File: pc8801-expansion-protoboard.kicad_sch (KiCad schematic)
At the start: 48 parts, among them J1 Solder Side, J10 CPOL select (to Fuji), J11 CPOL (Latch), J2 Parts Side, J3 5V, J4 12V, J5 -12V, J6 GND_1, J7 GND_2, J8 CPOL select (ESP)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

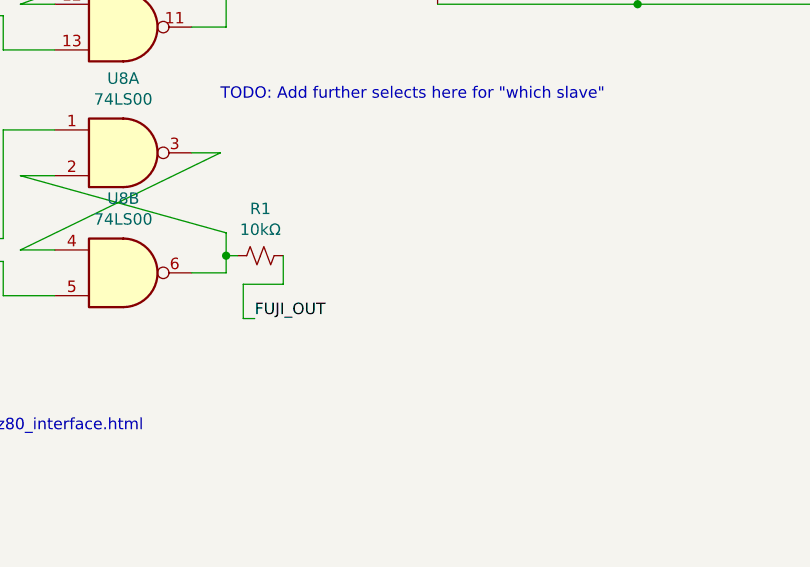
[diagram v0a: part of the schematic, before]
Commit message: Jumper to disable PU/PD
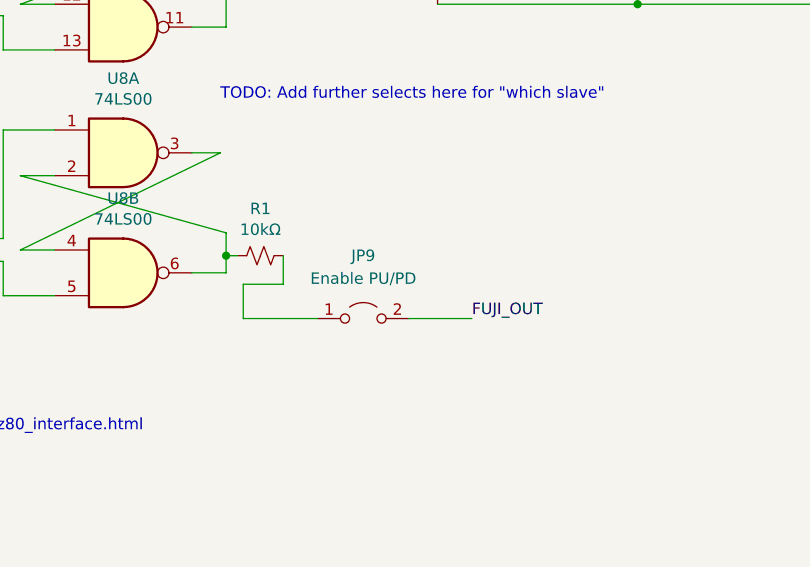
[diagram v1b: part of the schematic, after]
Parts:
- added JP9: Enable PU/PD, Connector_PinHeader_2.54mm:PinHeader_1x02_P2.54mm_Vertical, symbol Jumper:Jumper_2_Open
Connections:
- net FUJI_OUT: now also JP9.2 (B); no longer R1.2
- new net: JP9.1 (A), R1.2
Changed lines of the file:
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@@
+    (stroke (width 0) (type default) (color 0 0 0 0))
+  )
+  (wire (pts (xy 184.15 193.675) (xy 191.135 193.675))
     (stroke (width 0) (type default) (color 0 0 0 0))
   )
@@
     (stroke (width 0) (type default) (color 0 0 0 0))
   )
-  (wire (pts (xy 167.005 193.675) (xy 165.735 193.675))
+  (wire (pts (xy 165.735 193.675) (xy 173.99 193.675))
     (stroke (width 0) (type default) (color 0 0 0 0))
   )
@@
     (effects (font (size 1.27 1.27)) (justify left bottom))
   )
+  (label "FUJI_OUT" (at 191.135 193.675 0)
+    (effects (font (size 1.27 1.27)) (justify left bottom))
+  )
   (label "D1" (at 238.125 82.55 180)
     (effects (font (size 1.27 1.27)) (justify right bottom))
@@
   )
   (label "GND" (at 187.325 158.75 0)
-    (effects (font (size 1.27 1.27)) (justify left bottom))
-  )
-  (label "FUJI_OUT" (at 167.005 193.675 0)
     (effects (font (size 1.27 1.27)) (justify left bottom))
   )
@@
     (pin "3")
   )
+  (symbol (lib_id "Jumper:Jumper_2_Open") (at 179.07 193.675 0) (unit 1)
+    (in_bom yes) (on_board yes) (fields_autoplaced)
+    (property "Reference" "JP9" (id 0) (at 179.07 186.69 0))
+    (property "Value" "Enable PU/PD" (id 1) (at 179.07 189.23 0))
+    (property "Footprint" "Connector_PinHeader_2.54mm:PinHeader_1x02_P2.54mm_Vertical" (id 2) (at 179.07 193.675 0)
+      (effects (font (size 1.27 1.27)) hide)
+    )
+    (property "Datasheet" "~" (id 3) (at 179.07 193.675 0)
+      (effects (font (size 1.27 1.27)) hide)
+    )
+    (pin "1")
+    (pin "2")
+  )
   (symbol (lib_id "Device:D") (at 78.105 227.33 0) (unit 1)
     (in_bom yes) (on_board yes) (fields_autoplaced)
@@
       (reference "JP8") (unit 1) (value "Jumper_NC_Small") (footprint "Jumper:SolderJumper-2_P1.3mm_Bridged_RoundedPad1.0x1.5mm")
     )
+    (path "/a6a5797b-18fe-4a42-aa73-fdaee054c816"
+      (reference "JP9") (unit 1) (value "Enable PU/PD") (footprint "Connector_PinHeader_2.54mm:PinHeader_1x02_P2.54mm_Vertical")
+    )
     (path "/00000000-0000-0000-0000-000062ccaf1b"

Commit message: Test hooks for SPI clock
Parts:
- added TP3: SPI Clock, TestPoint:TestPoint_Loop_D2.60mm_Drill1.4mm_Beaded, symbol Connector:TestPoint
- added TP4: ~{SPI Clock}, TestPoint:TestPoint_Loop_D2.60mm_Drill1.4mm_Beaded, symbol Connector:TestPoint
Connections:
- net SPI_CLK: now also TP3.1
- net ~{SPI_CLK}: now also TP4.1
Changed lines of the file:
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@@
+    (stroke (width 0) (type default) (color 0 0 0 0))
+  )
+  (wire (pts (xy 271.78 30.48) (xy 271.78 36.195))
     (stroke (width 0) (type default) (color 0 0 0 0))
   )
@@
   )
   (wire (pts (xy 231.14 56.515) (xy 231.14 90.805))
+    (stroke (width 0) (type default) (color 0 0 0 0))
+  )
+  (wire (pts (xy 288.29 30.48) (xy 288.29 36.195))
     (stroke (width 0) (type default) (color 0 0 0 0))
   )
@@
     (effects (font (size 1.27 1.27)) (justify left bottom))
   )
+  (label "SPI_CLK" (at 271.78 36.195 270)
+    (effects (font (size 1.27 1.27)) (justify right bottom))
+  )
   (label "~{RESET}" (at 59.69 215.9 180)
     (effects (font (size 1.27 1.27)) (justify right bottom))
@@
   (label "GND" (at 254 120.65 0)
     (effects (font (size 1.27 1.27)) (justify left bottom))
+  )
+  (label "~{SPI_CLK}" (at 288.29 36.195 270)
+    (effects (font (size 1.27 1.27)) (justify right bottom))
   )
   (label "A0" (at 104.14 157.48 180)
@@
     (pin "1")
   )
+  (symbol (lib_id "Connector:TestPoint") (at 288.29 30.48 0) (unit 1)
+    (in_bom yes) (on_board yes) (fields_autoplaced)
+    (property "Reference" "TP4" (id 0) (at 290.83 25.9079 0)
+      (effects (font (size 1.27 1.27)) (justify left))
+    )
+    (property "Value" "~{SPI Clock}" (id 1) (at 290.83 29.0829 0)
+      (effects (font (size 1.27 1.27)) (justify left))
+    )
+    (property "Footprint" "TestPoint:TestPoint_Loop_D2.60mm_Drill1.4mm_Beaded" (id 2) (at 293.37 30.48 0)
+      (effects (font (size 1.27 1.27)) hide)
+    )
+    (property "Datasheet" "~" (id 3) (at 293.37 30.48 0)
+      (effects (font (size 1.27 1.27)) hide)
+    )
+    (pin "1")
+  )
   (symbol (lib_id "Connector:TestPoint") (at 63.5 27.305 0) (unit 1)
     (in_bom yes) (on_board yes) (fields_autoplaced)
@@
     (pin "2")
   )
+  (symbol (lib_id "Connector:TestPoint") (at 271.78 30.48 0) (unit 1)
+    (in_bom yes) (on_board yes) (fields_autoplaced)
+    (property "Reference" "TP3" (id 0) (at 274.32 25.9079 0)
+      (effects (font (size 1.27 1.27)) (justify left))
+    )
+    (property "Value" "SPI Clock" (id 1) (at 274.32 28.4479 0)
+      (effects (font (size 1.27 1.27)) (justify left))
+    )
+    (property "Footprint" "TestPoint:TestPoint_Loop_D2.60mm_Drill1.4mm_Beaded" (id 2) (at 276.86 30.48 0)
+      (effects (font (size 1.27 1.27)) hide)
+    )
+    (property "Datasheet" "~" (id 3) (at 276.86 30.48 0)
+      (effects (font (size 1.27 1.27)) hide)
+    )
+    (pin "1")
+  )
   (symbol (lib_id "Device:D") (at 78.105 227.33 0) (unit 1)
     (in_bom yes) (on_board yes) (fields_autoplaced)
@@
       (reference "TP2") (unit 1) (value "TestPoint") (footprint "TestPoint:TestPoint_Loop_D2.60mm_Drill1.4mm_Beaded")
     )
+    (path "/ce9231c3-ef0f-4298-8666-3e023bba7902"
+      (reference "TP3") (unit 1) (value "SPI Clock") (footprint "TestPoint:TestPoint_Loop_D2.60mm_Drill1.4mm_Beaded")
+    )
+    (path "/01b34e41-af93-4e1d-928b-489fa2be9377"
+      (reference "TP4") (unit 1) (value "~{SPI Clock}") (footprint "TestPoint:TestPoint_Loop_D2.60mm_Drill1.4mm_Beaded")
+    )
     (path "/00000000-0000-0000-0000-000061c04125"

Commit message: Series 220uF on 5V
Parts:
- added C?: 220µF, Capacitor_THT:CP_Radial_D5.0mm_P2.00mm, symbol Device:C_Polarized_Small_US
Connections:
- net +5V: now also C?.1; no longer J1.3 (Pin_3), J1.4 (Pin_4), J2.3 (Pin_3), J2.4 (Pin_4), U1.3A (+5V), U1.3B (+5V), U1.4A (+5V), U1.4B (+5V)
- new net 5V_RAW: C?.2, J1.3 (Pin_3), J1.4 (Pin_4), J2.3 (Pin_3), J2.4 (Pin_4), U1.3A (+5V), U1.3B (+5V), U1.4A (+5V), U1.4B (+5V)
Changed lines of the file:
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@@
   (junction (at 187.325 234.315) (diameter 0) (color 0 0 0 0)
   )
-  (junction (at 178.435 53.34) (diameter 0) (color 0 0 0 0)
-  )
   (junction (at 135.89 70.485) (diameter 0) (color 0 0 0 0)
   )
   (junction (at 51.435 140.97) (diameter 0) (color 0 0 0 0)
   )
+  (junction (at 122.555 52.705) (diameter 0) (color 0 0 0 0)
+  )
   (junction (at 158.75 47.625) (diameter 0) (color 0 0 0 0)
   )
@@
   (junction (at 282.575 74.295) (diameter 0) (color 0 0 0 0)
   )
-  (junction (at 122.555 52.705) (diameter 0) (color 0 0 0 0)
-  )
   (junction (at 158.75 106.045) (diameter 0) (color 0 0 0 0)
   )
@@
   (junction (at 250.825 120.65) (diameter 0) (color 0 0 0 0)
   )
+  (junction (at 97.155 36.195) (diameter 0) (color 0 0 0 0)
+  )
   (junction (at 135.89 65.405) (diameter 0) (color 0 0 0 0)
-  )
-  (junction (at 122.555 53.975) (diameter 0) (color 0 0 0 0)
   )
   (junction (at 82.55 257.81) (diameter 0) (color 0 0 0 0)
@@
     (stroke (width 0) (type default) (color 0 0 0 0))
   )
-  (wire (pts (xy 180.975 53.34) (xy 178.435 53.34))
-    (stroke (width 0) (type default) (color 0 0 0 0))
-  )
   (wire (pts (xy 129.54 160.02) (xy 139.065 160.02))
     (stroke (width 0) (type default) (color 0 0 0 0))
@@
     (stroke (width 0) (type default) (color 0 0 0 0))
   )
+  (wire (pts (xy 97.155 36.195) (xy 102.235 36.195))
+    (stroke (width 0) (type default) (color 0 0 0 0))
+  )
   (wire (pts (xy 167.005 124.46) (xy 167.005 128.905))
     (stroke (width 0) (type default) (color 0 0 0 0))
   )
+  (wire (pts (xy 93.345 36.195) (xy 97.155 36.195))
+    (stroke (width 0) (type default) (color 0 0 0 0))
+  )
   (wire (pts (xy 192.405 250.825) (xy 192.405 245.11))
     (stroke (width 0) (type default) (color 0 0 0 0))
@@
     (stroke (width 0) (type default) (color 0 0 0 0))
   )
-  (wire (pts (xy 122.555 55.245) (xy 122.555 53.975))
-    (stroke (width 0) (type default) (color 0 0 0 0))
-  )
   (wire (pts (xy 139.065 160.02) (xy 139.065 163.83))
     (stroke (width 0) (type default) (color 0 0 0 0))
@@
     (stroke (width 0) (type default) (color 0 0 0 0))
   )
-  (wire (pts (xy 120.015 53.975) (xy 122.555 53.975))
-    (stroke (width 0) (type default) (color 0 0 0 0))
-  )
   (wire (pts (xy 129.54 162.56) (xy 138.43 162.56))
     (stroke (width 0) (type default) (color 0 0 0 0))
@@
     (stroke (width 0) (type default) (color 0 0 0 0))
   )
-  (wire (pts (xy 178.435 55.245) (xy 178.435 53.34))
-    (stroke (width 0) (type default) (color 0 0 0 0))
-  )
   (wire (pts (xy 213.36 65.405) (xy 213.36 83.185))
     (stroke (width 0) (type default) (color 0 0 0 0))
@@
     (stroke (width 0) (type default) (color 0 0 0 0))
   )
+  (wire (pts (xy 122.555 36.195) (xy 122.555 52.705))
+    (stroke (width 0) (type default) (color 0 0 0 0))
+  )
   (wire (pts (xy 178.435 131.445) (xy 178.435 133.35))
     (stroke (width 0) (type default) (color 0 0 0 0))
@@
     (stroke (width 0) (type default) (color 0 0 0 0))
   )
+  (wire (pts (xy 107.315 36.195) (xy 122.555 36.195))
+    (stroke (width 0) (type default) (color 0 0 0 0))
+  )
   (wire (pts (xy 122.555 65.405) (xy 135.89 65.405))
     (stroke (width 0) (type default) (color 0 0 0 0))
@@
     (stroke (width 0) (type default) (color 0 0 0 0))
   )
-  (wire (pts (xy 178.435 53.34) (xy 178.435 52.705))
-    (stroke (width 0) (type default) (color 0 0 0 0))
-  )
-  (wire (pts (xy 122.555 53.975) (xy 122.555 52.705))
+  (wire (pts (xy 178.435 52.705) (xy 178.435 55.245))
+    (stroke (width 0) (type default) (color 0 0 0 0))
+  )
+  (wire (pts (xy 122.555 52.705) (xy 122.555 55.245))
     (stroke (width 0) (type default) (color 0 0 0 0))
   )
@@
     (effects (font (size 1.27 1.27)) (justify left bottom))
   )
+  (label "+5V" (at 93.345 36.195 180)
+    (effects (font (size 1.27 1.27)) (justify right bottom))
+  )
   (label "GND" (at 299.085 86.995 180)
     (effects (font (size 1.27 1.27)) (justify right bottom))
@@
     (effects (font (size 1.27 1.27)) (justify left bottom))
   )
-  (label "+5V" (at 120.015 53.975 180)
-    (effects (font (size 1.27 1.27)) (justify right bottom))
-  )
   (label "D7" (at 238.125 97.79 180)
     (effects (font (size 1.27 1.27)) (justify right bottom))
@@
     (effects (font (size 1.27 1.27)) (justify right bottom))
   )
+  (label "5V_RAW" (at 122.555 55.245 180)
+    (effects (font (size 1.27 1.27)) (justify right bottom))
+  )
   (label "~{SD_CS}" (at 302.26 97.155 0)
     (effects (font (size 1.27 1.27)) (justify left bottom))
@@
     (effects (font (size 1.27 1.27)) (justify left bottom))
   )
+  (label "5V_RAW" (at 178.435 52.705 0)
+    (effects (font (size 1.27 1.27)) (justify left bottom))
+  )
   (label "~{IOW}" (at 80.01 160.02 180)
     (effects (font (size 1.27 1.27)) (justify right bottom))
@@
   )
   (label "VSPI_SCK" (at 140.335 245.11 0)
-    (effects (font (size 1.27 1.27)) (justify left bottom))
-  )
-  (label "+5V" (at 180.975 53.34 0)
     (effects (font (size 1.27 1.27)) (justify left bottom))
   )
@@
     (pin "2")
   )
-  (symbol (lib_id "power:PWR_FLAG") (at 122.555 52.705 0) (unit 1)
-    (in_bom yes) (on_board yes)
-    (property "Reference" "#FLG0101" (id 0) (at 122.555 50.8 0)
-      (effects (font (size 1.27 1.27)) hide)
-    )
-    (property "Value" "PWR_FLAG" (id 1) (at 122.555 48.3108 0))
-    (property "Footprint" "" (id 2) (at 122.555 52.705 0)
-      (effects (font (size 1.27 1.27)) hide)
-    )
-    (property "Datasheet" "~" (id 3) (at 122.555 52.705 0)
+  (symbol (lib_id "power:PWR_FLAG") (at 97.155 36.195 0) (unit 1)
+    (in_bom yes) (on_board yes)
+    (property "Reference" "#FLG0101" (id 0) (at 97.155 34.29 0)
+      (effects (font (size 1.27 1.27)) hide)
+    )
+    (property "Value" "PWR_FLAG" (id 1) (at 97.155 31.8008 0)
+      (effects (font (size 1.27 1.27)) hide)
+    )
+    (property "Footprint" "" (id 2) (at 97.155 36.195 0)
+      (effects (font (size 1.27 1.27)) hide)
+    )
+    (property "Datasheet" "~" (id 3) (at 97.155 36.195 0)
       (effects (font (size 1.27 1.27)) hide)
     )
@@
     )
     (pin "1")
+  )
+  (symbol (lib_id "Device:C_Polarized_Small_US") (at 104.775 36.195 90) (unit 1)
+    (in_bom yes) (on_board yes) (fields_autoplaced)
+    (property "Reference" "C?" (id 0) (at 104.3432 29.21 90))
+    (property "Value" "220µF" (id 1) (at 104.3432 31.75 90))
+    (property "Footprint" "Capacitor_THT:CP_Radial_D5.0mm_P2.00mm" (id 2) (at 104.775 36.195 0)
+      (effects (font (size 1.27 1.27)) hide)
+    )
+    (property "Datasheet" "~" (id 3) (at 104.775 36.195 0)
+      (effects (font (size 1.27 1.27)) hide)
+    )
+    (pin "1")
+    (pin "2")
   )
   (symbol (lib_id "Connector:TestPoint") (at 63.5 27.305 0) (unit 1)
@@
       (reference "C4") (unit 1) (value "0.1µF") (footprint "Capacitor_THT:C_Disc_D5.0mm_W2.5mm_P2.50mm")
     )
+    (path "/039c2f34-b471-4ffe-a4c7-f26dfdac7f6f"
+      (reference "C?") (unit 1) (value "220µF") (footprint "Capacitor_THT:CP_Radial_D5.0mm_P2.00mm")
+    )
     (path "/79af274b-03a2-4947-b1c3-eb23d037fb00"
